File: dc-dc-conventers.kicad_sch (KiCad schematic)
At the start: 113 parts

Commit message: Fixed U45 direction issue
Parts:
- C183, C184, C185, C186: value (none) -> C_10u_25V_0603; footprint (none) -> kria-k26-devboard-footprints:0603-cap
- C187, C188: value (none) -> C_1u_0402; footprint (none) -> kria-k26-devboard-footprints:0402-cap
- C189, C190: value (none) -> C_3n9_0402; footprint (none) -> kria-k26-devboard-footprints:0402-cap
- C191, C192: value (none) -> C_100n_0402; footprint (none) -> kria-k26-devboard-footprints:0402-cap
- C193, C194: value (none) -> C_22p_0402; footprint (none) -> kria-k26-devboard-footprints:0402-cap
- C195, C196, C197, C198, C199, C200: value (none) -> C_22u_0603; footprint (none) -> kria-k26-devboard-footprints:0603-cap
- C201, C202, C203, C204, C205, C219, C220: renamed from C?; value (none) -> C_10u_25V_0603; footprint (none) -> kria-k26-devboard-footprints:0603-cap
- C206, C207, C208, C209, C210, C221, C222: renamed from C?; value (none) -> C_100n_0402; footprint (none) -> kria-k26-devboard-footprints:0402-cap
- C211, C212, C213, C214, C215, C216, C217, C218, C223, C224, C225, C226: renamed from C?; value (none) -> C_22u_0603; footprint (none) -> kria-k26-devboard-footprints:0603-cap
- D12, D13, D14, D15, D16, D17, D18, D19, D20: value (none) -> LG_L29K-G2J1-24-Z; footprint (none) -> kria-k26-devboard-footprints:LED_0603
- L1, L2: value (none) -> XEL4030-332MEC; footprint (none) -> kria-k26-devboard-footprints:Coilcraft-XEL4030
- L3: renamed from L?; value (none) -> XEL4030-222MEC; footprint (none) -> kria-k26-devboard-footprints:Coilcraft-XEL4030
- L4, L7: value (none) -> TFM201208ALD-1R0MTCA; footprint (none) -> antmicro-footprints:0805-res
- L5, L6, L8, L9: renamed from L?; value (none) -> SRP2010-1R0M; footprint (none) -> kria-k26-devboard-footprints:INDC2016X100N
- Q13, Q14, Q15: value (none) -> DTC014TEBTL; footprint (none) -> kria-k26-devboard-footprints:SOT-416
- R118, R119: value (none) -> R_100k_0402; footprint (none) -> kria-k26-devboard-footprints:0402-res
- R120, R121: value (none) -> R_2k_0402; footprint (none) -> kria-k26-devboard-footprints:0402-res
- R122, R124: value (none) -> R_147k_0402; footprint (none) -> kria-k26-devboard-footprints:0402-res
- R123, R125: value (none) -> R_24k_0402; footprint (none) -> kria-k26-devboard-footprints:0402-res
- R126, R130, R141, R142, R143: value (none) -> R_1k_0402; footprint (none) -> kria-k26-devboard-footprints:0402-res
- R127: value (none) -> R_0R_0402; footprint (none) -> kria-k26-devboard-footprints:0402-res
- R128: value (none) -> R_510R_0402; footprint (none) -> kria-k26-devboard-footprints:0402-res
- R129: value (none) -> R_68_0402; footprint (none) -> kria-k26-devboard-footprints:0402-res
- R131, R144: renamed from R?; value (none) -> R_31k6_0402; footprint (none) -> kria-k26-devboard-footprints:0402-res
- R132, R134, R136, R138, R140, R145, R147: renamed from R?; value (none) -> R_10k_0402; footprint (none) -> kria-k26-devboard-footprints:0402-res
- R133: renamed from R?; value (none) -> R_21k5_0402; footprint (none) -> kria-k26-devboard-footprints:0402-res
- R135: renamed from R?; value (none) -> R_12k4_0402; footprint (none) -> kria-k26-devboard-footprints:0402-res
- R137, R146: renamed from R?; value (none) -> R_4k99_0402; footprint (none) -> kria-k26-devboard-footprints:0402-res
- R139: renamed from R?; value (none) -> R_2k49_0402; footprint (none) -> kria-k26-devboard-footprints:0402-res
- TP36, TP37, TP38, TP39, TP40, TP41, TP42, TP50, TP51: value (none) -> TP_SMD_0_75MM; footprint (none) -> kria-k26-devboard-footprints:Testpoint_smd_0_75mm
- U47, U48: value (none) -> RT6236AHGQUF; footprint (none) -> kria-k26-devboard-footprints:RICHTEK_13-UFQFN
- U49, U50, U51, U52, U53, U54, U55: renamed from U?; value (none) -> AP62301WU-7; footprint (none) -> kria-k26-devboard-footprints:TSOT23-6

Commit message: Loclib of project in KiCad 6 format. Removed old KiCad 5 files
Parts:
- L4, L7: footprint antmicro-footprints:0805-res -> kria-k26-devboard-footprints:0805-res; symbol antmicroFixedInductors:TFM201208ALD-1R0MTCA -> kria-k26-devboard:TFM201208ALD-1R0MTCA

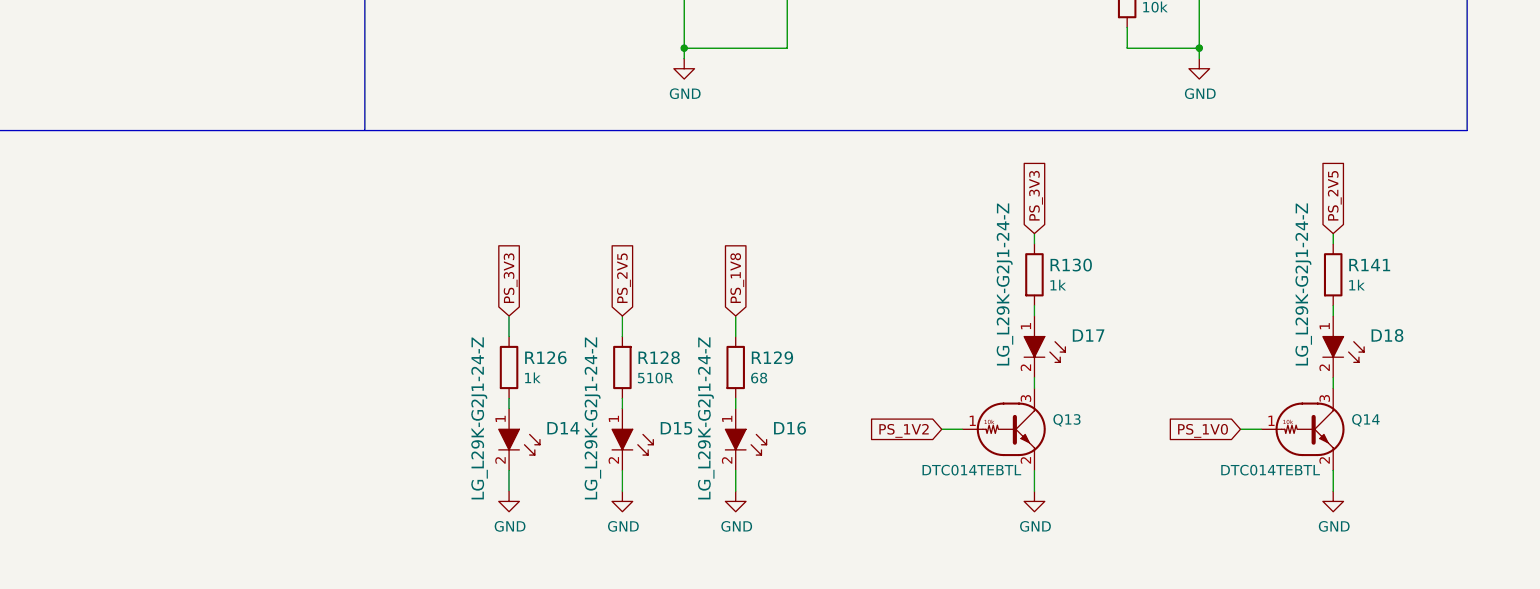
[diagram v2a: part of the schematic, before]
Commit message: Unified indication LED intensity
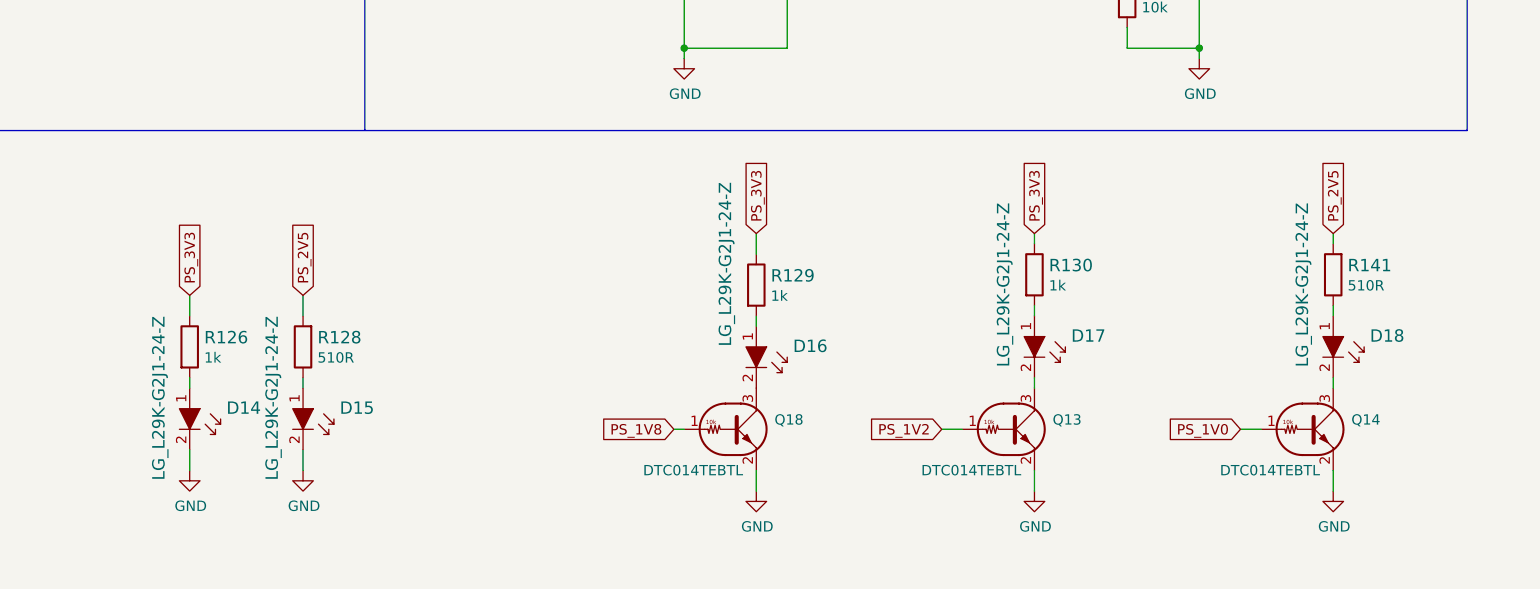
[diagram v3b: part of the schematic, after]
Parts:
- removed R129: R_68_0402, kria-k26-devboard-footprints:0402-res, symbol kria-k26-devboard:R_68_0402
- removed R141: R_1k_0402, kria-k26-devboard-footprints:0402-res, symbol kria-k26-devboard:R_1k_0402
- added Q18: DTC014TEBTL, kria-k26-devboard-footprints:SOT-416, symbol kria-k26-devboard:DTC014TEBTL
- added R129: R_1k_0402, kria-k26-devboard-footprints:0402-res, symbol kria-k26-devboard:R_1k_0402
- added R141: R_510R_0402, kria-k26-devboard-footprints:0402-res, symbol kria-k26-devboard:R_510R_0402
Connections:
- net GND: now also Q18.2 (E); no longer D16.2
- net PS_1V8: now also Q18.1 (B)
- net PS_2V5: now also R141.2
- net PS_3V3: now also R129.1
- net at D16.1: now also R129.2
- net at D18.1: now also R141.1
- new net: D16.2, Q18.3 (C)
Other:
- moved on the sheet: D14, D15, D16, R126, R128

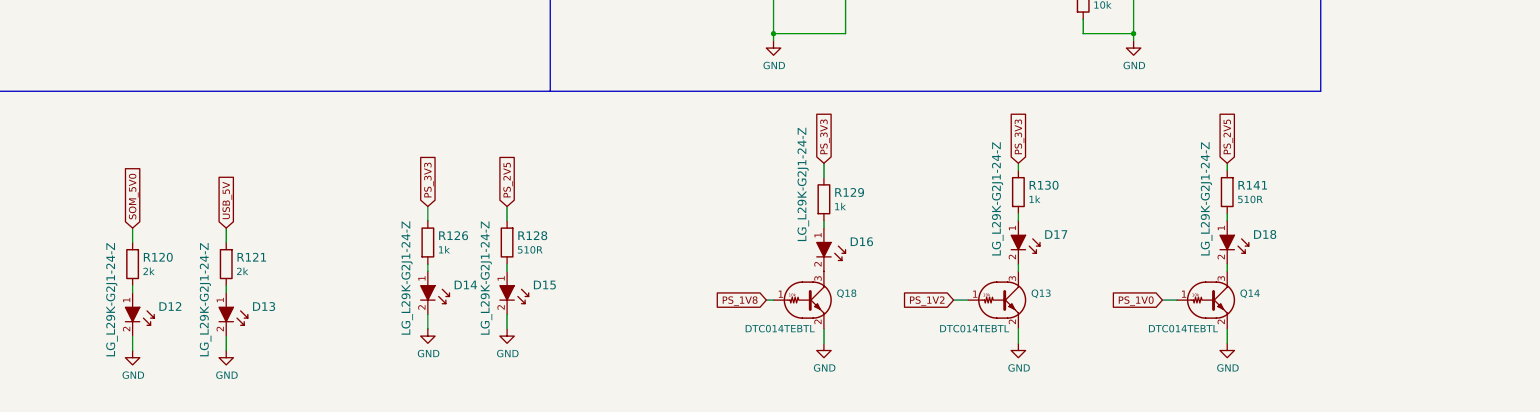
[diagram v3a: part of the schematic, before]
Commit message: Added Antmicro and OSHW logos o schematics. Removed one more file from KiCad 5 version
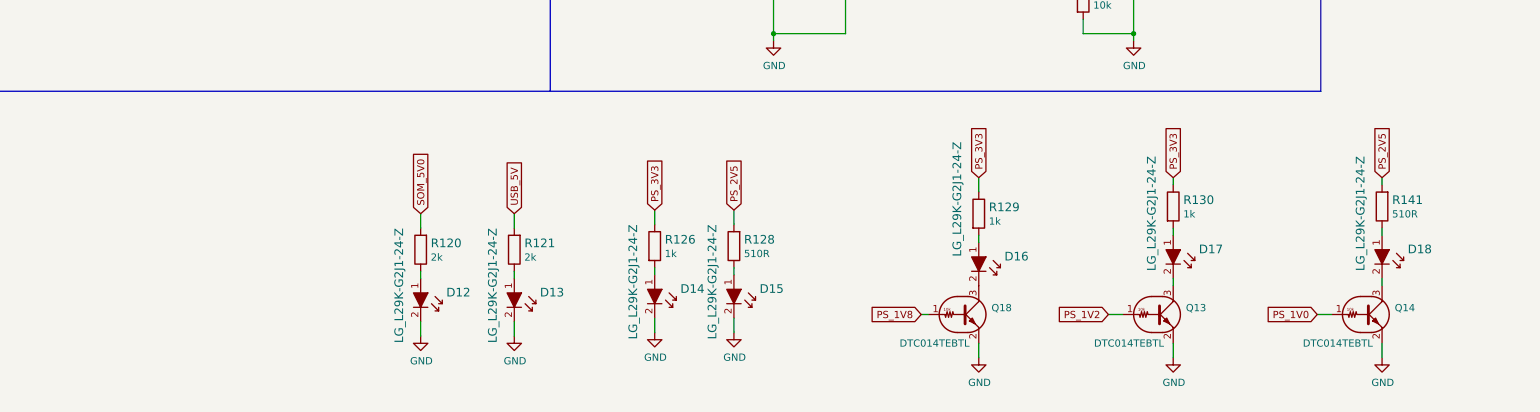
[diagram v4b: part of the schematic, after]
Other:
- moved on the sheet: D12, D13, D14, D15, D16, D17, D18, Q13, Q14, Q18, R120, R121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

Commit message: Several cosmetic changes. Corrected R177, R122, R124. Loclib
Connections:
- net SOM_5V0: now also R124.1
- net USB_5V: now also R122.1
- net at C193.1, R123.1, U47.3 (FB): now also R122.2
- net at C194.1, R125.1, U48.3 (FB): now also R124.2
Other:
- moved on the sheet: C195, C197, C199, TP51
